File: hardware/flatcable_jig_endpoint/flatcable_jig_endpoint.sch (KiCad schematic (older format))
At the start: 17 parts, among them J1 Coax, J3 Conn_01x03, J4 Conn_01x03, J5 Conn_02x05_Odd_Even

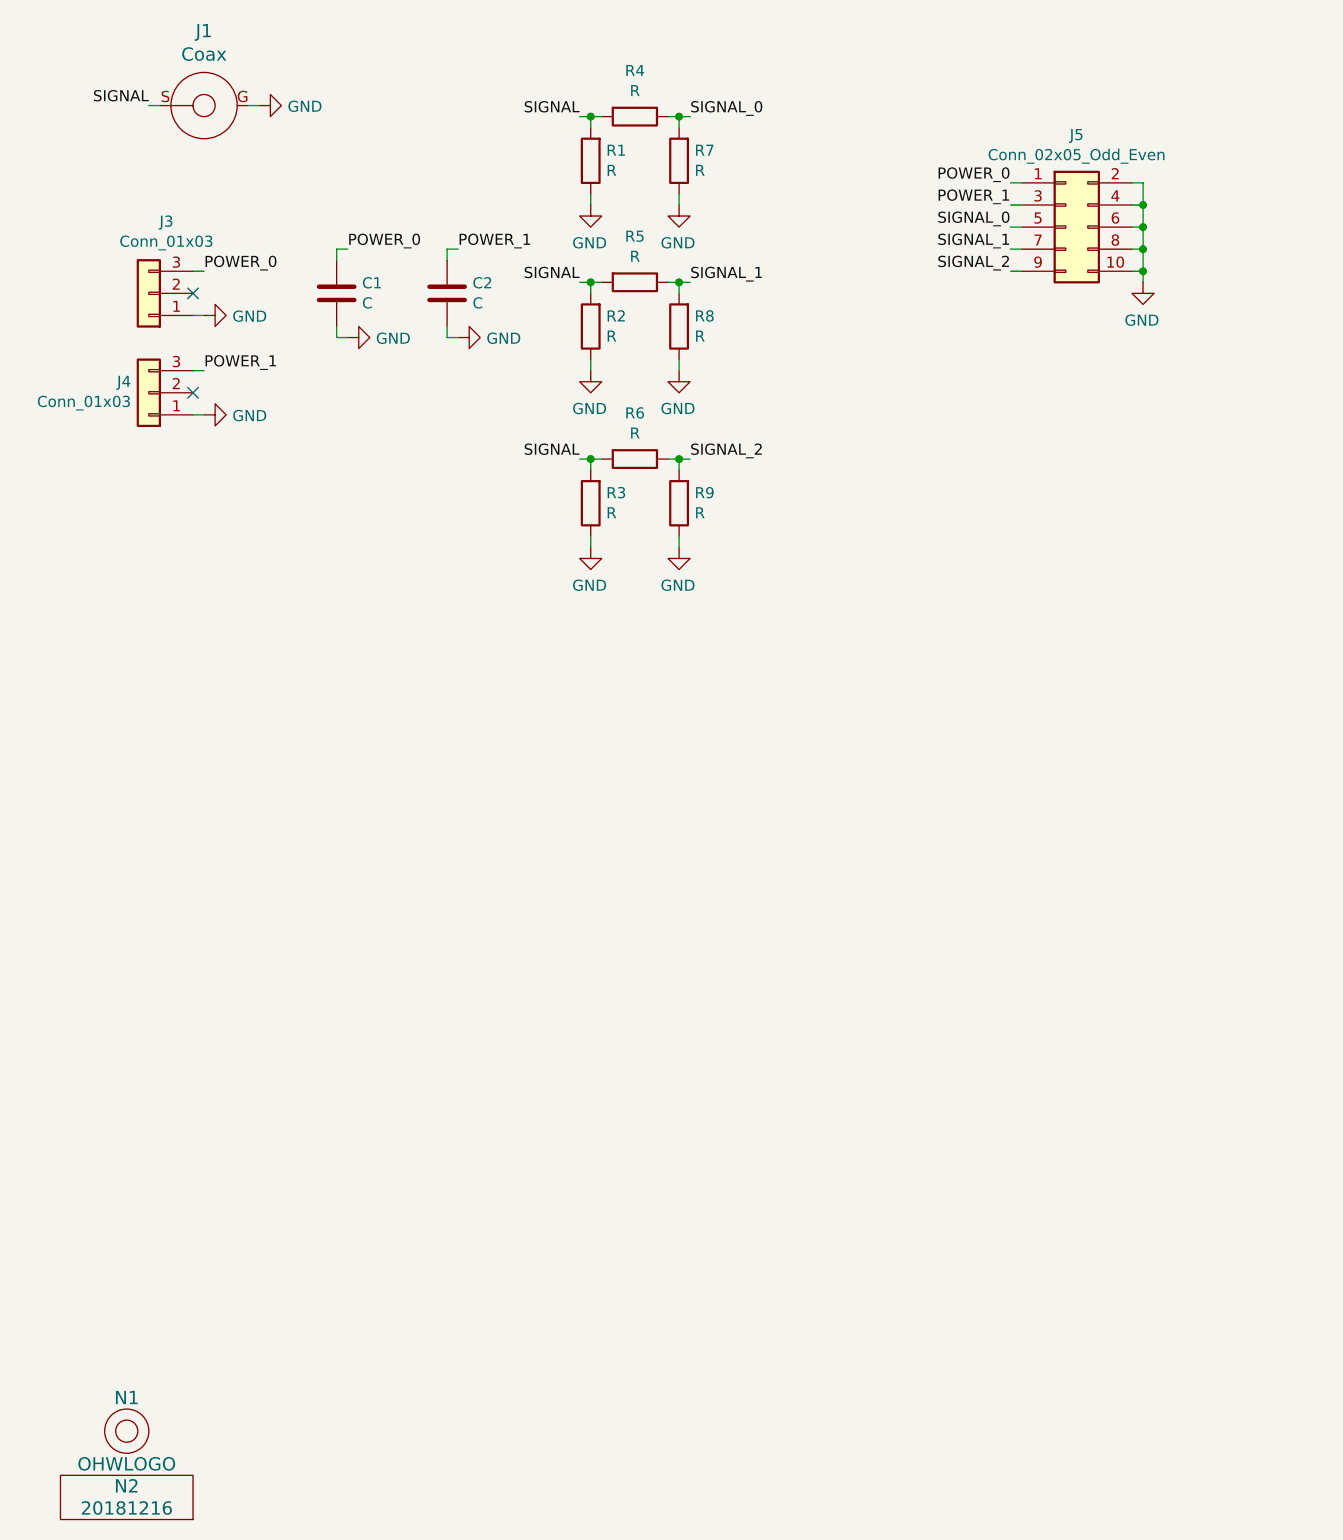
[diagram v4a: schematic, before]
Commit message: added jumperable grounds
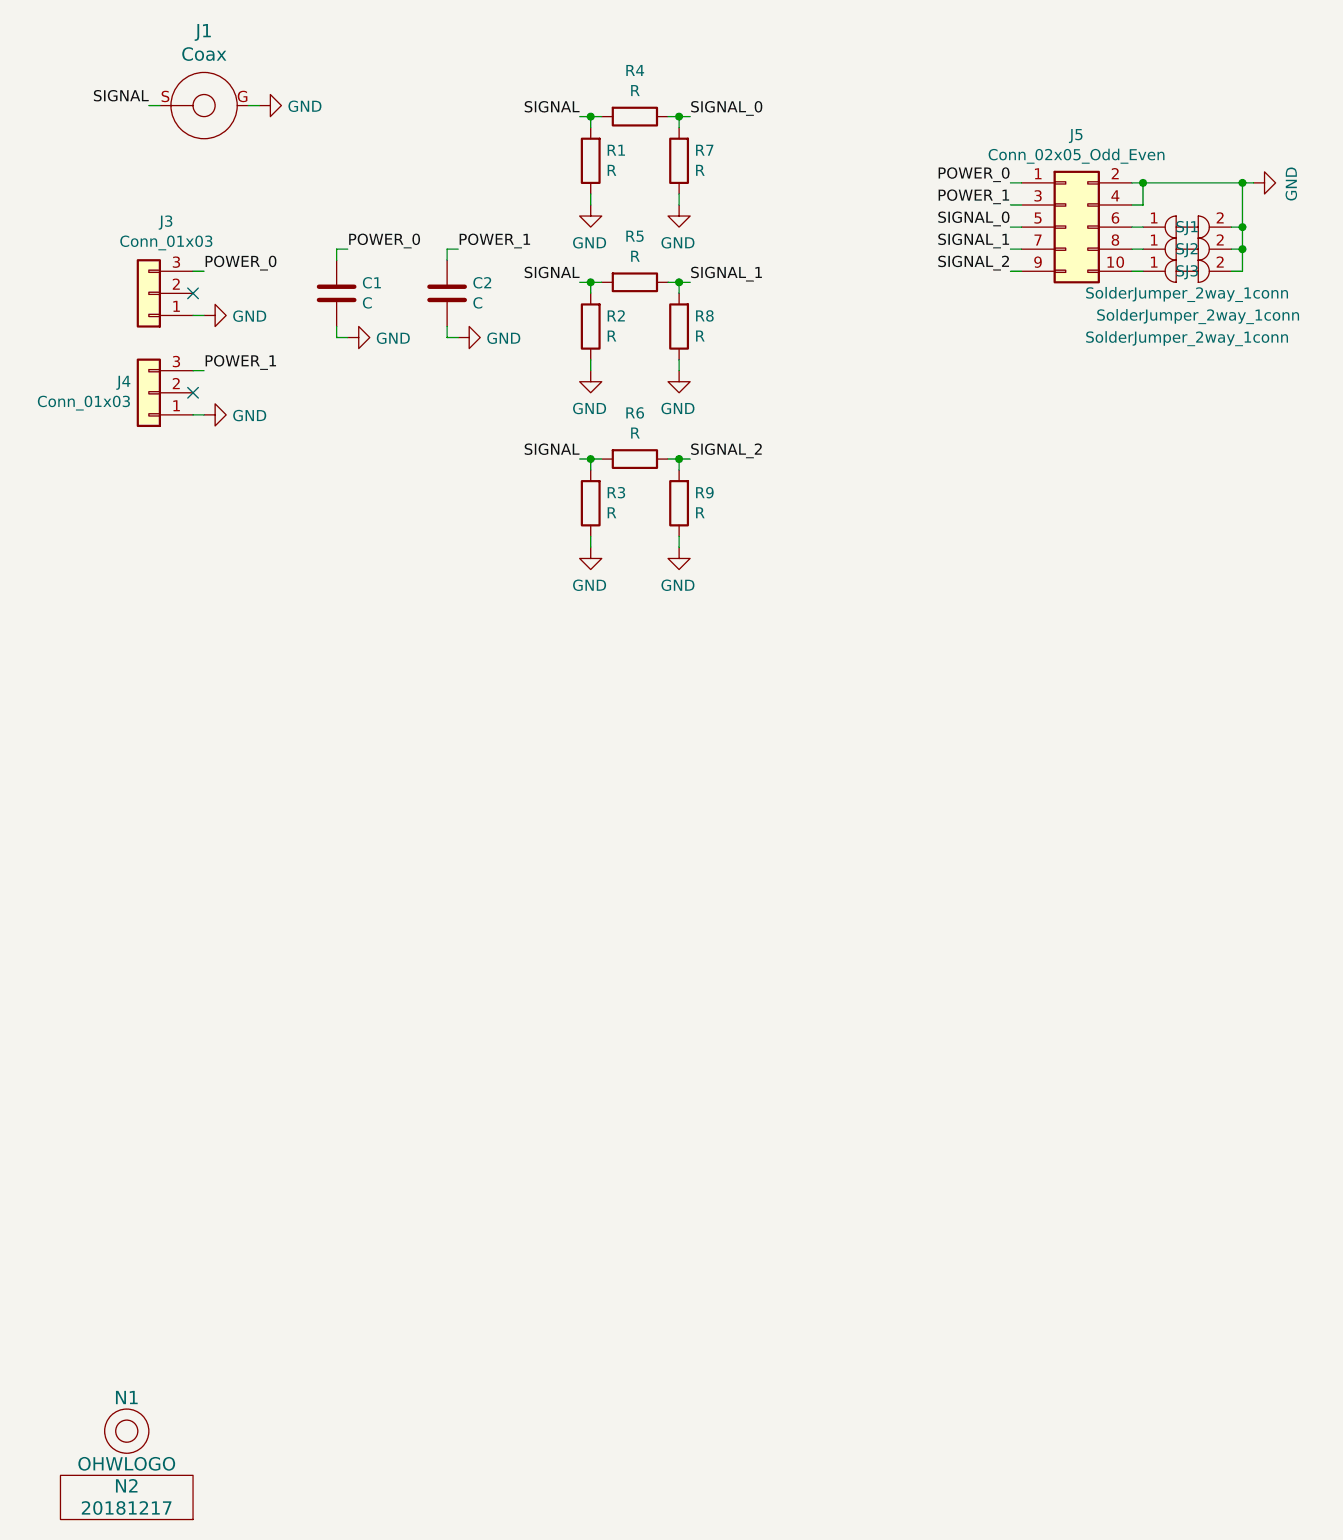
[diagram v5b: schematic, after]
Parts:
- added SJ1, SJ2, SJ3: SolderJumper_2way_1conn, SquantorSpecial:solder_jumper_2way_conn, symbol SquantorSpecial:SolderJumper_2way_1conn
- N2: value 20181216 -> 20181217
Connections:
- net GND: now also SJ1.2, SJ2.2, SJ3.2; no longer J5.10 (Pin_10), J5.6 (Pin_6), J5.8 (Pin_8)
- new net: J5.10 (Pin_10), SJ3.1
- new net: J5.6 (Pin_6), SJ1.1
- new net: J5.8 (Pin_8), SJ2.1
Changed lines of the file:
@@
 P 850 7700
 F 0 "N2" H 850 7800 60  0000 C CNN
-F 1 "20181216" H 850 7700 60  0000 C CNN
+F 1 "20181217" H 850 7700 60  0000 C CNN
 F 2 "SquantorLabels:Label_version" H 850 7700 60  0001 C CNN
 F 3 "" H 850 7700 60  0001 C CNN
@@
 L power:GND #PWR0104
 U 1 1 5C14E4F7
-P 5450 2150
-F 0 "#PWR0104" H 5450 1900 50  0001 C CNN
-F 1 "GND" H 5455 1977 50  0000 C CNN
-F 2 "" H 5450 2150 50  0001 C CNN
-F 3 "" H 5450 2150 50  0001 C CNN
-	1    5450 2150
-	-1   0    0    -1
-$EndComp
-Wire Wire Line
-	5400 1700 5450 1700
-Wire Wire Line
-	5450 1700 5450 1800
-Wire Wire Line
-	5400 2100 5450 2100
-Connection ~ 5450 2100
-Wire Wire Line
-	5450 2100 5450 2150
-Wire Wire Line
-	5400 2000 5450 2000
-Connection ~ 5450 2000
-Wire Wire Line
-	5450 2000 5450 2100
-Wire Wire Line
-	5400 1900 5450 1900
-Connection ~ 5450 1900
-Wire Wire Line
-	5450 1900 5450 2000
-Wire Wire Line
-	5400 1800 5450 1800
-Connection ~ 5450 1800
-Wire Wire Line
-	5450 1800 5450 1900
+P 5950 1700
+F 0 "#PWR0104" H 5950 1450 50  0001 C CNN
+F 1 "GND" H 5955 1527 50  0000 C CNN
+F 2 "" H 5950 1700 50  0001 C CNN
+F 3 "" H 5950 1700 50  0001 C CNN
+	1    5950 1700
+	0    -1   1    0
+$EndComp
 Wire Wire Line
 	4900 1700 4850 1700
@@
 Wire Wire Line
 	1400 1350 1450 1350
+Wire Wire Line
+	5400 1800 5450 1800
+Wire Wire Line
+	5450 1800 5450 1700
+Wire Wire Line
+	5450 1700 5900 1700
+Wire Wire Line
+	5450 1700 5400 1700
+Connection ~ 5450 1700
+$Comp
+L SquantorSpecial:SolderJumper_2way_1conn SJ1
+U 1 1 5C18966E
+P 5650 1900
+F 0 "SJ1" H 5650 1900 50  0000 C CNN
+F 1 "SolderJumper_2way_1conn" H 5650 1400 50  0000 C CNN
+F 2 "SquantorSpecial:solder_jumper_2way_conn" H 5650 1900 50  0001 C CNN
+F 3 "" H 5650 1900 50  0001 C CNN
+	1    5650 1900
+	1    0    0    -1
+$EndComp
+$Comp
+L SquantorSpecial:SolderJumper_2way_1conn SJ2
+U 1 1 5C1897A6
+P 5650 2000
+F 0 "SJ2" H 5650 2000 50  0000 C CNN
+F 1 "SolderJumper_2way_1conn" H 5700 1700 50  0000 C CNN
+F 2 "SquantorSpecial:solder_jumper_2way_conn" H 5650 2000 50  0001 C CNN
+F 3 "" H 5650 2000 50  0001 C CNN
+	1    5650 2000
+	1    0    0    -1
+$EndComp
+$Comp
+L SquantorSpecial:SolderJumper_2way_1conn SJ3
+U 1 1 5C1897DC
+P 5650 2100
+F 0 "SJ3" H 5650 2100 50  0000 C CNN
+F 1 "SolderJumper_2way_1conn" H 5650 2000 50  0000 C CNN
+F 2 "SquantorSpecial:solder_jumper_2way_conn" H 5650 2100 50  0001 C CNN
+F 3 "" H 5650 2100 50  0001 C CNN
+	1    5650 2100
+	1    0    0    -1
+$EndComp
+Wire Wire Line
+	5850 1900 5900 1900
+Wire Wire Line
+	5900 1900 5900 1700
+Connection ~ 5900 1700
+Wire Wire Line
+	5900 1700 5950 1700
+Wire Wire Line
+	5850 2100 5900 2100
+Wire Wire Line
+	5900 2100 5900 2000
+Connection ~ 5900 1900
+Wire Wire Line
+	5850 2000 5900 2000
+Connection ~ 5900 2000
+Wire Wire Line
+	5900 2000 5900 1900
+Wire Wire Line
+	5400 1900 5450 1900
+Wire Wire Line
+	5450 2000 5400 2000
+Wire Wire Line
+	5400 2100 5450 2100
 $EndSCHEMATC

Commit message: updated versionnumbers, no real changes actually
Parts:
- N2: value 20181217 -> 20190121
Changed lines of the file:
@@
 P 850 7700
 F 0 "N2" H 850 7800 60  0000 C CNN
-F 1 "20181217" H 850 7700 60  0000 C CNN
+F 1 "20190121" H 850 7700 60  0000 C CNN
 F 2 "SquantorLabels:Label_version" H 850 7700 60  0001 C CNN
 F 3 "" H 850 7700 60  0001 C CNN
